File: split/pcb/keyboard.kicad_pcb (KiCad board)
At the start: 2 copper layers, 173.5 x 126 mm, 116 parts, among them J1 TRRS, J2 IO

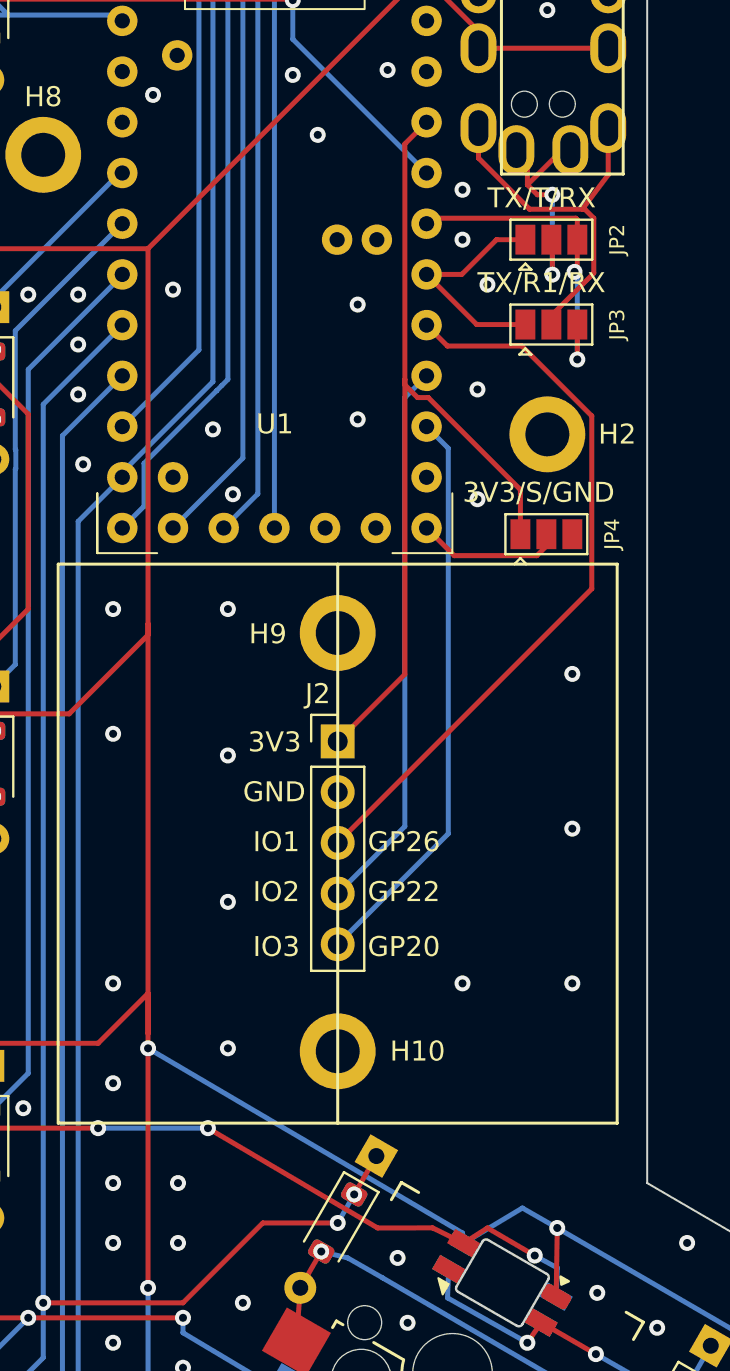
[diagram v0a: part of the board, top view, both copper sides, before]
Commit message: fix accessory connector
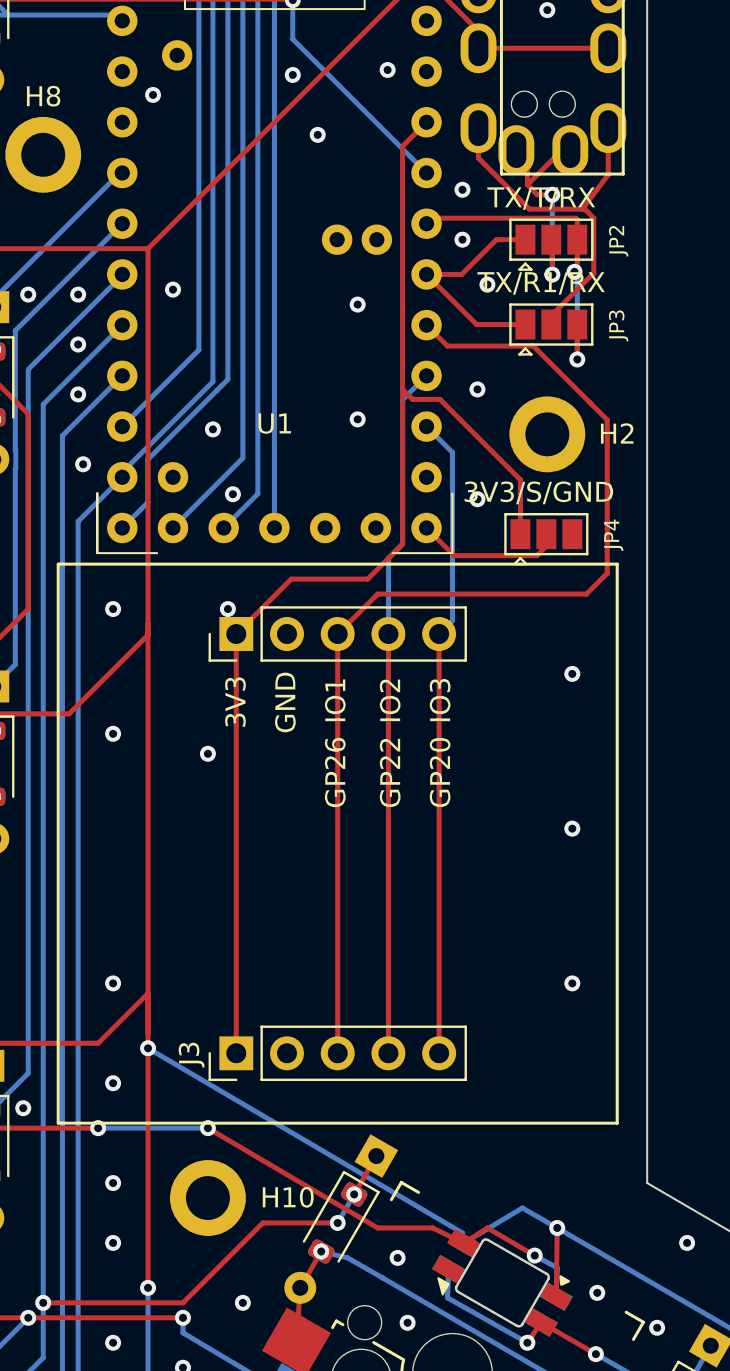
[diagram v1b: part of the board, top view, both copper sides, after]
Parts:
- removed H9: MountingHole_Pad_MP, MountingHole:MountingHole_2.2mm_M2_DIN965_Pad
- added J3: IO, Connector_PinHeader_2.54mm:PinHeader_1x05_P2.54mm_Vertical, F.Cu at (308.2, 205.8)
- moved H10 9.81 mm to (306.8, 213.0)
- moved J2 7.40 mm to (308.2, 184.8), turned to 90 degrees
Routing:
- net 3V3: track 42.9 -> 63.3 mm
- net IO1: track 36.4 -> 54.6 mm
- net IO2: track 27.4 -> 34.7 mm
- net unconnected-(D33-DOUT-Pad1)_1: track 7.24 -> 0.00 mm, vias 1 -> 0
- net unconnected-(D33-DOUT-Pad1): track 0.00 -> 7.24 mm, vias 0 -> 1
- net IO3: track 28.3 -> 32.2 mm
- net GND: track 0.37 -> 0.67 mm, vias 271 -> 266

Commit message: pcb fixes
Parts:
- removed JP2: T_SEL, Jumper:SolderJumper-3_P1.3mm_Open_Pad1.0x1.5mm
- removed JP3: R1_SEL, Jumper:SolderJumper-3_P1.3mm_Open_Pad1.0x1.5mm
- added JP1: SolderJumper_2_Open, Jumper:SolderJumper-2_P1.3mm_Open_Pad1.0x1.5mm, F.Cu at (323.0, 167.2)
- D1: moved to B.Cu
- J2, J3: footprint Connector_PinHeader_2.54mm:PinHeader_1x05_P2.54mm_Vertical -> Connector_PinHeader_2.54mm:PinHeader_1x07_P2.54mm_Vertical
- moved J1 3.25 mm to (319.6, 158.5)
- moved U1 3.22 mm to (301.2, 177.5)
- moved J2 2.50 mm to (305.7, 184.8)
- moved J3 2.50 mm to (305.7, 205.8)
- turned D1 to 180 degrees
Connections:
- J1 pad R1: Net-(JP3-C) -> RX
- J1 pad T: Net-(JP2-C) -> TX
- J2 pad 2: GND -> LED_POWER
- J2 pad 3: IO1 -> GND
- J2 pad 4: IO2 -> IO1
- J2 pad 5: IO3 -> IO2
- J3 pad 2: GND -> LED_POWER
- J3 pad 3: IO1 -> GND
- J3 pad 4: IO2 -> IO1
- J3 pad 5: IO3 -> IO2
- U1 pad 23: unconnected-(U1-GP23-Pad23) -> IO4
- U1 pad BOOT: unconnected-(U1-PadBOOT) -> Net-(JP1-A)
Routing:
- net LED_POWER: track 956.3 -> 989.9 mm, vias 36 -> 37
- net IO4: track 0.00 -> 33.4 mm
- net Net-(JP1-A): track 0.00 -> 25.7 mm, vias 0 -> 2
- net Net-(JP3-C): track 18.8 -> 0.00 mm
- net Net-(JP2-C): track 10.8 -> 0.00 mm, vias 2 -> 0
- net unconnected-(D33-DOUT-Pad1): track 7.24 -> 0.00 mm, vias 1 -> 0
- net 3V3: track 63.3 -> 69.6 mm
- net col5: track 238.6 -> 232.7 mm
- net IO2: track 34.7 -> 39.7 mm
- net col3: track 330.7 -> 326.0 mm
- net col2: track 283.0 -> 278.6 mm
- net col1: track 301.3 -> 297.3 mm, vias 15 -> 17
- net IO3: track 32.2 -> 35.9 mm
- net col0: track 322.4 -> 318.8 mm
- net row1: track 139.9 -> 143.5 mm
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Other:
- board text added: "5V"
- board text added: "BOOT"
- board text added: "GP23"
- board text added: "IO4"
- board text removed: "TX/R1/RX"
- board text removed: "TX/T/RX"

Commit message: closer thumbcluster, more layout
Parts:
- moved H7 11.0 mm to (318.8, 262.8)
- moved D25 10.3 mm to (311.5, 219.8)
- moved D26 10.3 mm to (328.2, 229.5)
- moved D27 10.3 mm to (319.2, 245.5)
- moved D28 10.3 mm to (302.2, 235.8)
- moved D_29 10.3 mm to (303.2, 216.8)
- moved D_30 10.3 mm to (320.0, 226.2)
- moved D_31 10.3 mm to (294.0, 232.2)
- moved D_32 10.3 mm to (310.8, 242.5)
- moved K_29 10.3 mm to (309.0, 224.3)
- moved K_30 10.3 mm to (325.6, 234.0)
- moved K_31 10.3 mm to (299.6, 240.0)
- moved K_32 10.3 mm to (316.5, 250.0)
- moved H5 10.2 mm to (338.0, 228.8)
- moved H10 6.50 mm to (313.2, 213.0)
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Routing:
- net row4: track 205.3 -> 194.4 mm
- net col3: track 326.0 -> 315.4 mm, vias 17 -> 16
- net Net-(D28-DOUT): track 44.6 -> 35.4 mm
- net col5: track 232.7 -> 223.7 mm, vias 16 -> 17
- net LED_POWER: track 989.9 -> 982.2 mm
- net Net-(D24-DOUT): track 45.8 -> 39.3 mm, vias 4 -> 2
- net col4: track 343.1 -> 341.0 mm
- net row5: track 111.6 -> 109.5 mm
- net GND: vias 284 -> 273
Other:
- board size 173.5 x 126 mm -> 163.5 x 129.2 mm
